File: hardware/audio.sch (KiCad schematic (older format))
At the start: 37 parts, among them U1 74HC4053, U2 TL072, U3 IS31AP2110

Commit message: Schematic mainly done. Working on PCB layout in isolated blocks.
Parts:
- removed C1, C15, C16, C2, C3, C5, C6, C7: 1u0, Capacitor_SMD:C_0603_1608Metric, symbol Device:C_Small
- removed C? (x3): 10n, Capacitor_SMD:C_0603_1608Metric, symbol Device:C_Small
- removed L1, L? (x3): 15u, symbol Device:L
- removed R1, R2: R_Small, Resistor_SMD:R_0603_1608Metric, symbol Device:R_Small
- removed U2: TL072, Package_SO:SOIC-8_3.9x4.9mm_P1.27mm, symbol Amplifier_Operational:TL072
- removed U3: IS31AP2110, Package_SO:TSSOP-28-1EP_4.4x9.7mm_P0.65mm, symbol Console2JAMMA:IS31AP2110
- added C39, C40: 1u0, Capacitor_SMD:C_0805_2012Metric, symbol Device:C_Small
- added C41, C42, C55, C56, C78, C79: 10u, Capacitor_SMD:C_0805_2012Metric, symbol Device:C_Small
- added C43, C44, C52, C60, C65: 100n, Capacitor_SMD:C_0603_1608Metric, symbol Device:C_Small
- added C45, C46, C47, C48, C49, C54, C59: 1u0, Capacitor_SMD:C_0603_1608Metric, symbol Device:C_Small
- added C50: 100u, Capacitor_SMD:CP_Elec_8x10.5, symbol Device:CP1_Small
- added C57: 10n, Capacitor_SMD:C_0603_1608Metric, symbol Device:C_Small
- added C61, C62, C63, C64: 220n, Capacitor_SMD:C_1210_3225Metric, symbol Device:C_Small
- added JP1, JP2: SolderJumper_3_Bridged12, Jumper:SolderJumper-3_P1.3mm_Bridged12_Pad1.0x1.5mm, symbol Jumper:SolderJumper_3_Bridged12
- added L1, L2, L3, L4: 15u, Inductor_SMD:L_10.4x10.4_H4.8, symbol Device:L_Small
- added R15: 2K, Resistor_SMD:R_0603_1608Metric, symbol Device:R_Small
- added R22, R23: 10K, Resistor_SMD:R_0603_1608Metric, symbol Device:R_Small
- added R24, R25: R_Small, Resistor_SMD:R_0603_1608Metric, symbol Device:R_Small
- added R26: 100K, Resistor_SMD:R_0603_1608Metric, symbol Device:R_Small
- added R27, R28, R29: 4K7, Resistor_SMD:R_0603_1608Metric, symbol Device:R_Small
- added U12: TL074, Package_SO:TSSOP-14_4.4x5mm_P0.65mm, symbol Amplifier_Operational:TL074
- added U13: LM1972, Package_SO:SOIC-20W_7.5x12.8mm_P1.27mm, symbol Console2JAMMA:LM1972
- added U14: TPA3138D2, Package_SO:TSSOP-28-1EP_4.4x9.7mm_P0.65mm, symbol Console2JAMMA:TPA3138D2
- C66: renamed from C20; footprint Capacitor_SMD:C_0603_1608Metric -> Capacitor_SMD:C_1210_3225Metric
- C67, C68, C69: renamed from C?; footprint Capacitor_SMD:C_0603_1608Metric -> Capacitor_SMD:C_1210_3225Metric
- U15: renamed from U1; value 74HC4053 -> 74HCT4053; footprint Package_SO:TSSOP-14_4.4x5mm_P0.65mm -> Package_SO:SSOP-16_5.3x6.2mm_P0.65mm
- renumbered C11 to C37, C12 to C38, C10 to C51, C14 to C53, C18 to C58, C4 to C73, C8 to C77, R3 to R16, R4 to R17, R5 to R18, R6 to R19, R7 to R20, R8 to R21
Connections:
- net labels added: +3V3, Audio_L_Mono, VOL_CLK, VOL_DATA_IN, VOL_LOAD_SHIFT
- net labels removed: -12V, Audio_L_OR_Mono
- wire segments 122 -> 224
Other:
- note added: "1SPW"
- note added: "20dB"
- note added: "26dB"
- note added: "Amplifier & Volume Control"
- note added: "BD"
- note removed: "Audio Amplifier"
- moved on the sheet: C37, C38, C51, C53, C58, C66, C67, C68, C69, C73, C77, R16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

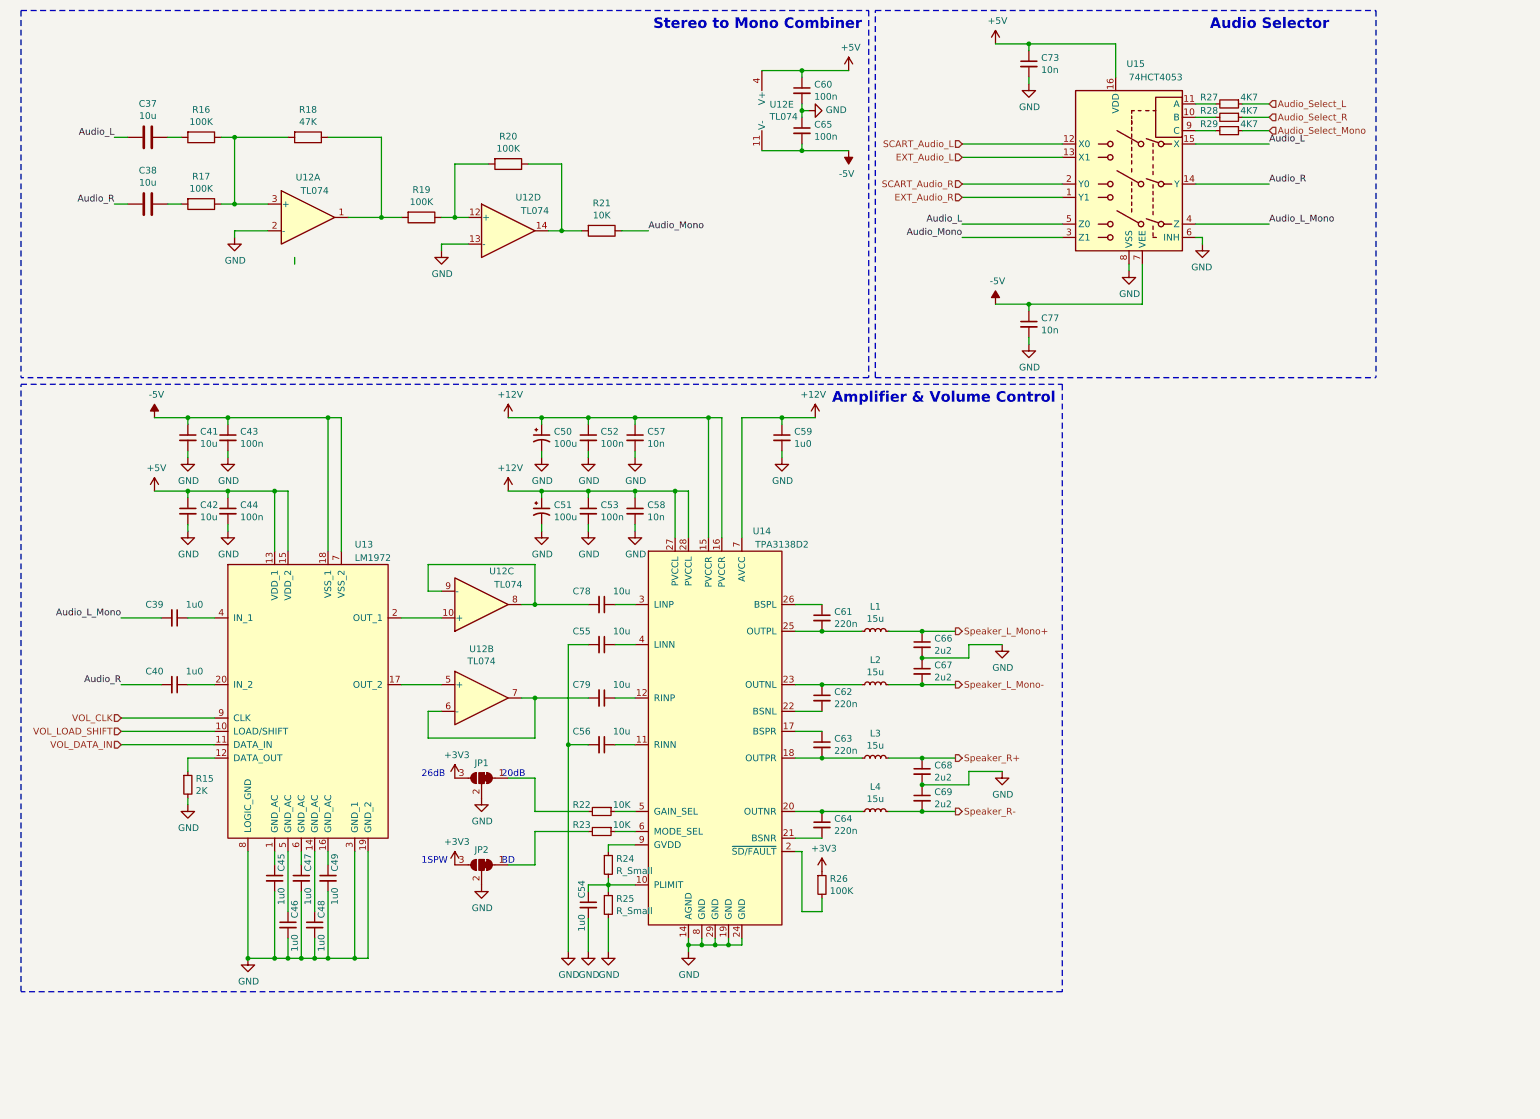
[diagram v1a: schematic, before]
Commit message: Completing the functionality of PCB layout. Require silkscreen placement still, though.
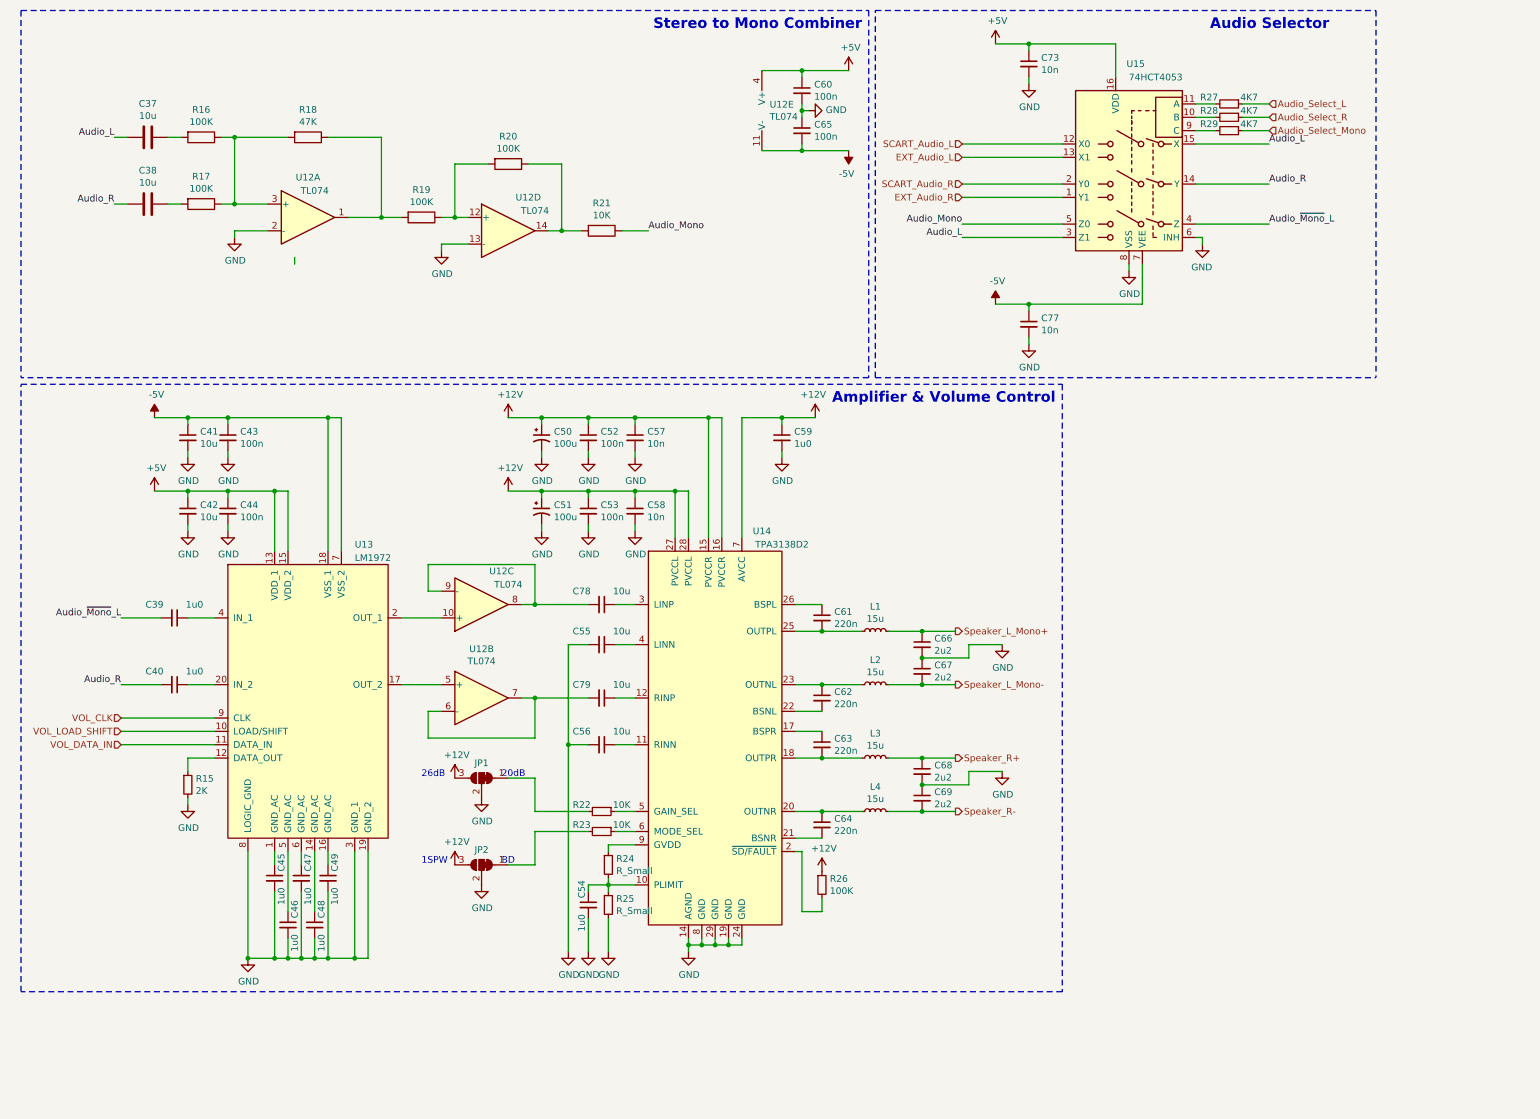
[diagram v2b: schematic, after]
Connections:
- net +3V3 is gone; now on net +12V: JP1.3 (B), JP2.3 (B), R26.1
- net Audio_L: now also U15.3 (Z1); no longer U15.5 (Z0)
- net Audio_Mono: now also U15.5 (Z0); no longer U15.3 (Z1)
- net Audio_L_Mono renamed Audio_~Mono~_L
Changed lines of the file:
@@
 $Descr A3 16535 11693
 encoding utf-8
-Sheet 4 4
-Title "Audio Section"
-Date "2020-04-03"
+Sheet 3 4
+Title "JAMMA2Console"
+Date "2020-04-06"
 Rev "1"
 Comp "Gold"
@@
 Wire Wire Line
 	9350 2150 9900 2150
+Text Label 7600 2250 2    50   ~ 0
+Audio_L
 Text Label 7600 2150 2    50   ~ 0
-Audio_L
-Text Label 7600 2250 2    50   ~ 0
 Audio_Mono
 Wire Wire Line
@@
 	9350 1250 9500 1250
 Text Label 9900 2150 0    50   ~ 0
-Audio_L_Mono
+Audio_~Mono~_L
 Wire Wire Line
 	8850 2450 8850 2500
@@
 Stereo to Mono Combiner
 $Comp
-L power:+3V3 #PWR0105
-U 1 1 5ED13A6A
-P 3800 6950
-F 0 "#PWR0105" H 3800 6800 50  0001 C CNN
-F 1 "+3V3" H 3815 7123 50  0000 C CNN
-F 2 "" H 3800 6950 50  0001 C CNN
-F 3 "" H 3800 6950 50  0001 C CNN
-	1    3800 6950
-	1    0    0    -1
-$EndComp
-$Comp
 L power:GND #PWR0106
 U 1 1 5EB61EA7
@@
 Text Notes 4150 6950 0    50   ~ 0
 BD
-$Comp
-L power:+3V3 #PWR0104
-U 1 1 5ECD0E42
-P 3800 6300
-F 0 "#PWR0104" H 3800 6150 50  0001 C CNN
-F 1 "+3V3" H 3815 6473 50  0000 C CNN
-F 2 "" H 3800 6300 50  0001 C CNN
-F 3 "" H 3800 6300 50  0001 C CNN
-	1    3800 6300
-	1    0    0    -1
-$EndComp
 $Comp
 L Jumper:SolderJumper_3_Bridged12 JP1
@@
 VOL_DATA_IN
 Text Label 1300 5100 2    50   ~ 0
-Audio_L_Mono
+Audio_~Mono~_L
 Wire Wire Line
 	1300 5100 1600 5100
@@
 Wire Notes Line
 	550  550  550  3300
-$Comp
-L power:+3V3 #PWR0123
-U 1 1 5E8426E2
-P 6550 7000
-F 0 "#PWR0123" H 6550 6850 50  0001 C CNN
-F 1 "+3V3" H 6565 7173 50  0000 C CNN
-F 2 "" H 6550 7000 50  0001 C CNN
-F 3 "" H 6550 7000 50  0001 C CNN
-	1    6550 7000
-	1    0    0    -1
-$EndComp
 Wire Wire Line
 	6350 6850 6400 6850
@@
 Wire Wire Line
 	7600 2250 8350 2250
+$Comp
+L power:+12V #PWR0104
+U 1 1 5EAC0C6E
+P 6550 7000
+F 0 "#PWR0104" H 6550 6850 50  0001 C CNN
+F 1 "+12V" H 6565 7173 50  0000 C CNN
+F 2 "" H 6550 7000 50  0001 C CNN
+F 3 "" H 6550 7000 50  0001 C CNN
+	1    6550 7000
+	1    0    0    -1
+$EndComp
+$Comp
+L power:+12V #PWR0105
+U 1 1 5EAD9DB9
+P 3800 6300
+F 0 "#PWR0105" H 3800 6150 50  0001 C CNN
+F 1 "+12V" H 3815 6473 50  0000 C CNN
+F 2 "" H 3800 6300 50  0001 C CNN
+F 3 "" H 3800 6300 50  0001 C CNN
+	1    3800 6300
+	1    0    0    -1
+$EndComp
+$Comp
+L power:+12V #PWR0123
+U 1 1 5EADA1FC
+P 3800 6950
+F 0 "#PWR0123" H 3800 6800 50  0001 C CNN
+F 1 "+12V" H 3815 7123 50  0000 C CNN
+F 2 "" H 3800 6950 50  0001 C CNN
+F 3 "" H 3800 6950 50  0001 C CNN
+	1    3800 6950
+	1    0    0    -1
+$EndComp
 $EndSCHEMATC

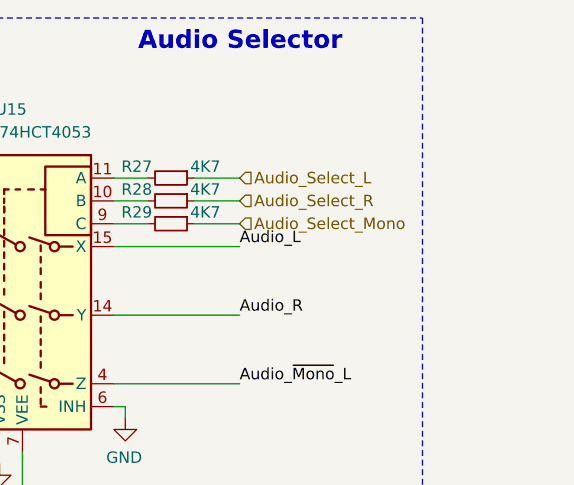
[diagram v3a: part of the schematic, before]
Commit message: Completing layout & minor edits for the main PCB. Added a project for the adapters to plug controllers into.
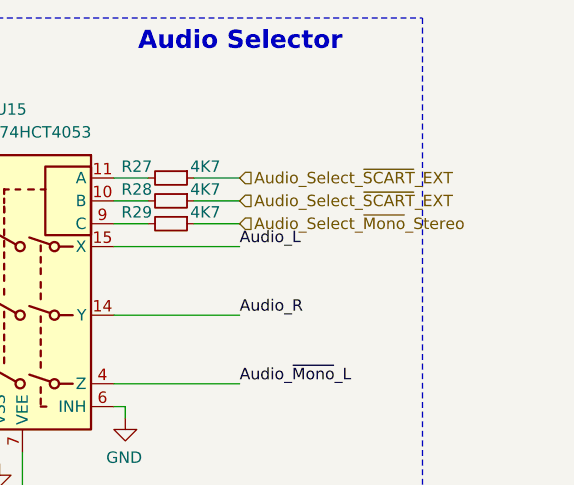
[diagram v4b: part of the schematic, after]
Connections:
- net Audio_Select_R is gone; now on net Audio_Select_~SCART~_EXT: R28.1
- net Audio_Select_L renamed Audio_Select_~SCART~_EXT
- net Audio_Select_Mono renamed Audio_Select_~Mono~_Stereo
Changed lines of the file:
@@
 	1    0    0    -1
 $EndComp
-Text HLabel 9900 1250 2    50   Input ~ 0
-Audio_Select_L
-Text HLabel 9900 1350 2    50   Input ~ 0
-Audio_Select_R
-Text HLabel 9900 1450 2    50   Input ~ 0
-Audio_Select_Mono
 Text Label 9900 1550 0    50   ~ 0
 Audio_L
@@
 	1    0    0    -1
 $EndComp
+Text HLabel 9900 1250 2    50   Input ~ 0
+Audio_Select_~SCART~_EXT
+Text HLabel 9900 1350 2    50   Input ~ 0
+Audio_Select_~SCART~_EXT
+Text HLabel 9900 1450 2    50   Input ~ 0
+Audio_Select_~Mono~_Stereo
 $EndSCHEMATC
